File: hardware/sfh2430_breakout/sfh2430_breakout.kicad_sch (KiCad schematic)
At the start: 6 parts, among them J2 Conn_01x10, U1 LTC2052IS_PBF

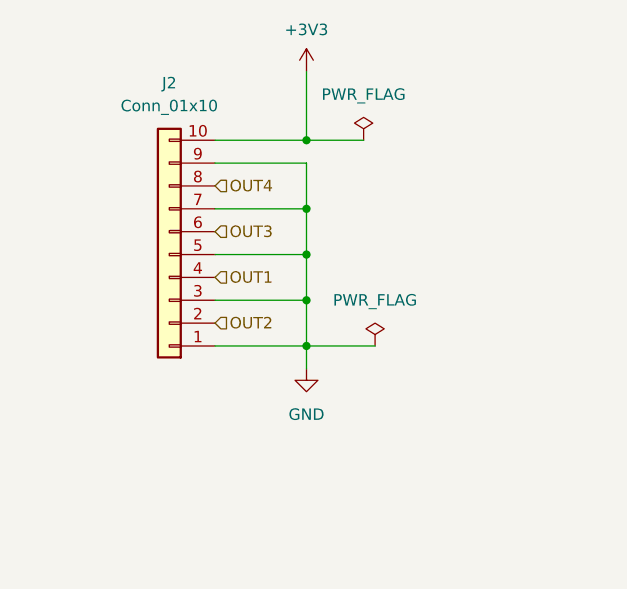
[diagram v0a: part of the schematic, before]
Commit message: add PiCoral 1.0.0
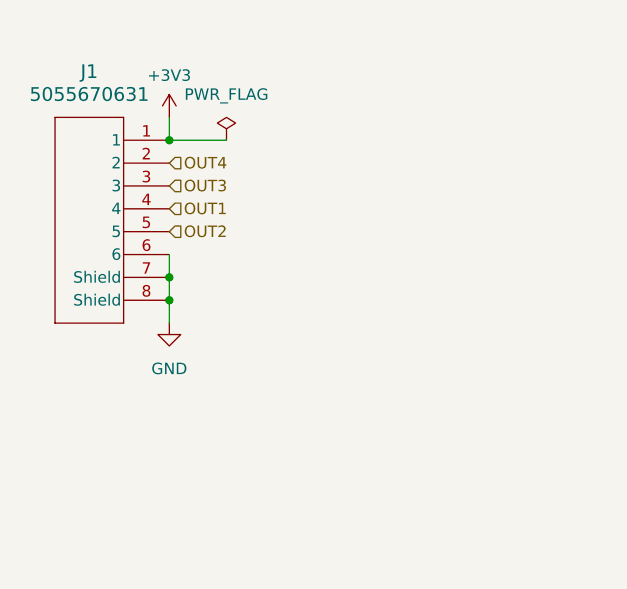
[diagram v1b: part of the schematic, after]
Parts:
- removed J2: Conn_01x10, adcs:10pin_1mm_pitch_flat_flex, symbol Connector_Generic:Conn_01x10
- added J1: 5055670631, adcs:CON_5055670631, symbol adcs:5055670631
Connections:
- net +3V3: now also J1.1
- net GND: now also J1.6, J1.7 (Shield), J1.8 (Shield)
- net OUT1: now also J1.4
- net OUT2: now also J1.5
- net OUT3: now also J1.3
- net OUT4: now also J1.2
